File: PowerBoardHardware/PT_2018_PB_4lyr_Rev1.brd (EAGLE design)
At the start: 177.8 x 209.6 mm, 250 parts, among them J1 APP_2POS_CONFIG12V_VERT, J2 APP_2POS_CONFIG12V_VERT, J3 APP_2POS_CONFIG12V_VERT, J4 RJ45KEYSTONE-942, J5 APP_2POS_CONFIGMOCO_VERT, J6 JTAG_ARM_10PIN, Q1 Q_IRFS7437PbF, Q10 Q_IRFS7437PbF, Q11 2N7002, Q12 2N7002, Q13 2N7002PW, Q14 2N7002PW, Q2 Q_IRFS7437PbF, Q3 Q_IRFS7437PbF, Q4 Q_IRFS7437PbF, Q5 MOSFET-NCHANNELFDD8780, Q6 Q_IRFS7437PbF, Q7 Q_IRFS7437PbF, Q8 MOSFET-NCHANNELFDD8780, Q9 Q_IRFS7437PbF, U1 ACS722LLCTR-40AU-T, U10 LT1910, U11 LT1910, U12 ACS722LLCTR-40AU-T, U13 LT1910, U14 ACS722LLCTR-40AU-T, U15 LT1910, U16 LT1910, U17 ACS722LLCTR-40AU-T, U18 ACS722LLCTR-40AU-T, U19 LT1910, U2 ACS722LLCTR-40AU-T, U20 LT1910, U21 SLVU2.8-4, U22 HX1198FNL, U23 MAX3232D, U3 LT1910, U4 ACS722LLCTR-40AU-T, U5 LT1910, U6 ACS722LLCTR-40AU-T, U7 LT1910, U8 ACS722LLCTR-40AU-T, U9 ACS722LLCTR-40AU-T, Y1 CRYATL_32K_SMD, Y2 NX3225GA

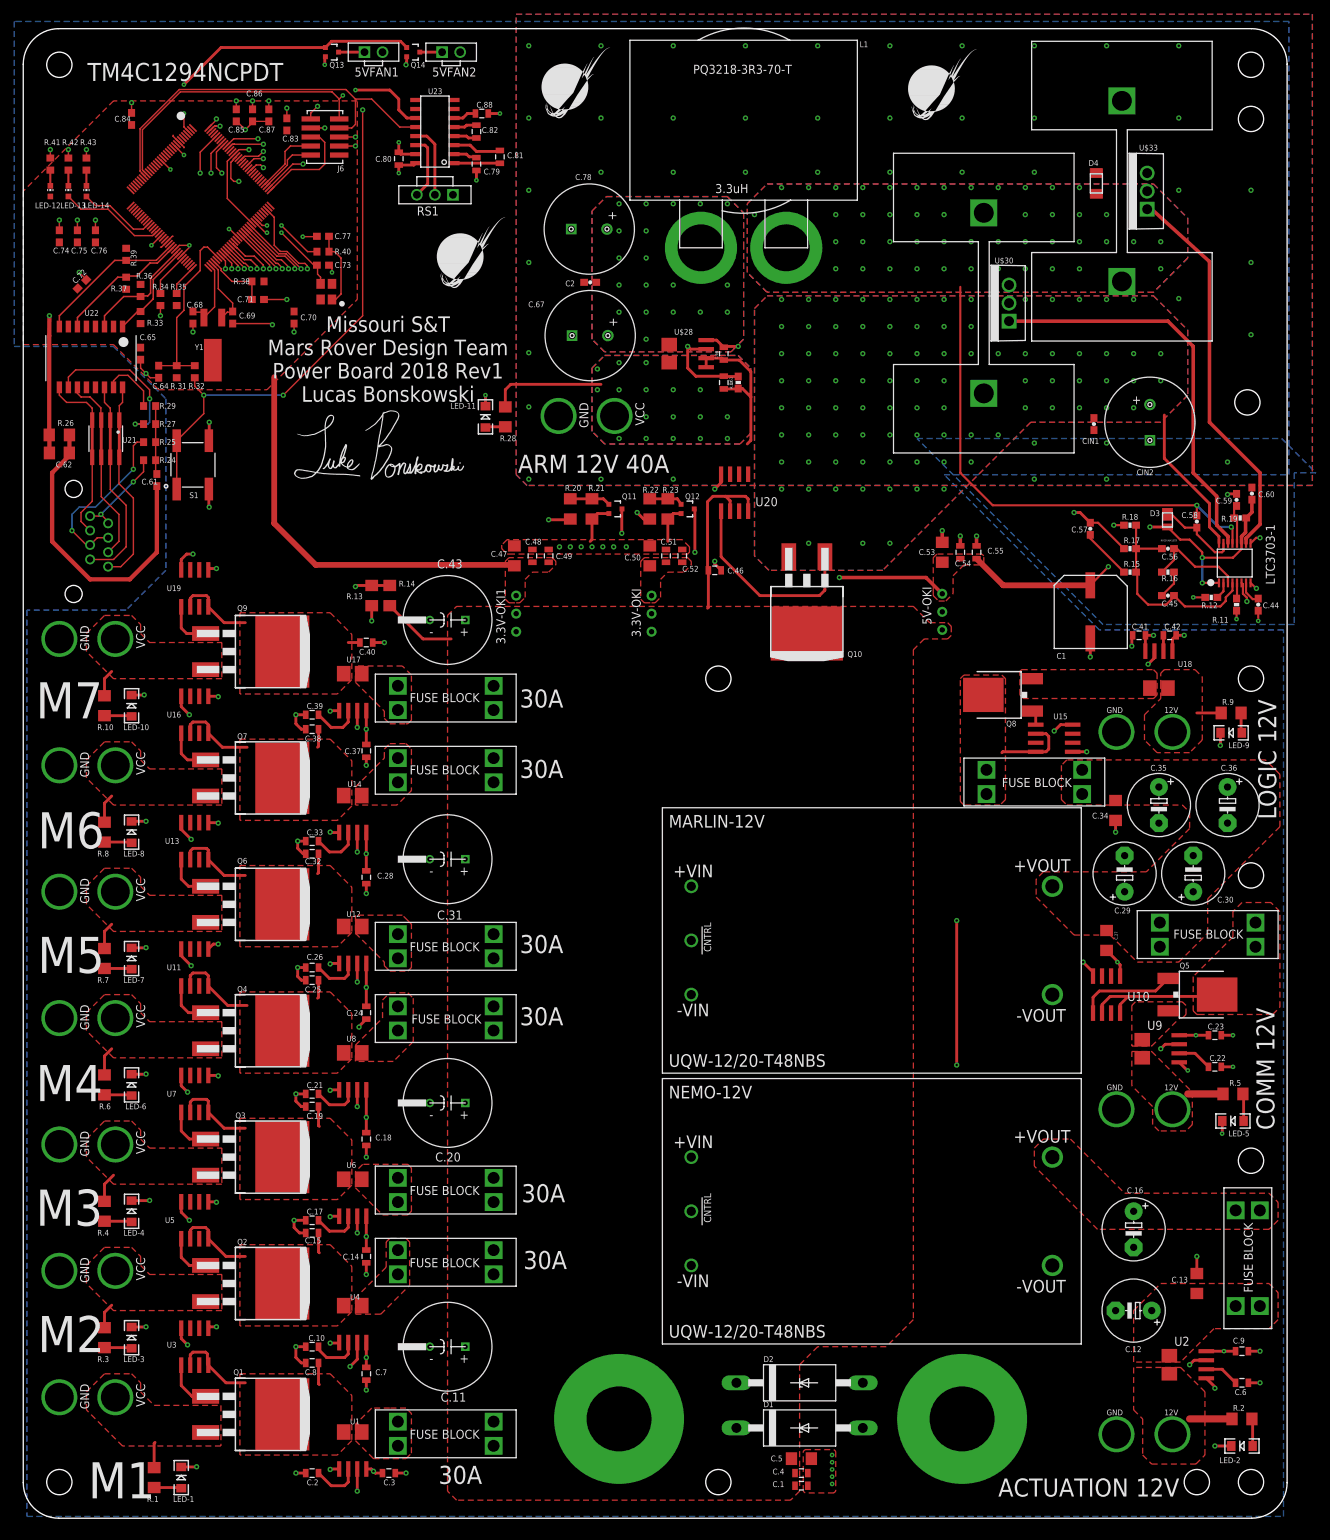
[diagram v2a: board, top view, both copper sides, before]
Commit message: FINAL REV 1 TO BE ORDERED
Made ground plane around buck converter 4 layers. Adjusted via stitch to allow 3.3v plane to have a larger bottleneck.  Flipped logic and comm bus locations.  Added + and - near battery terminals. Renumbered components since we missed a few before.
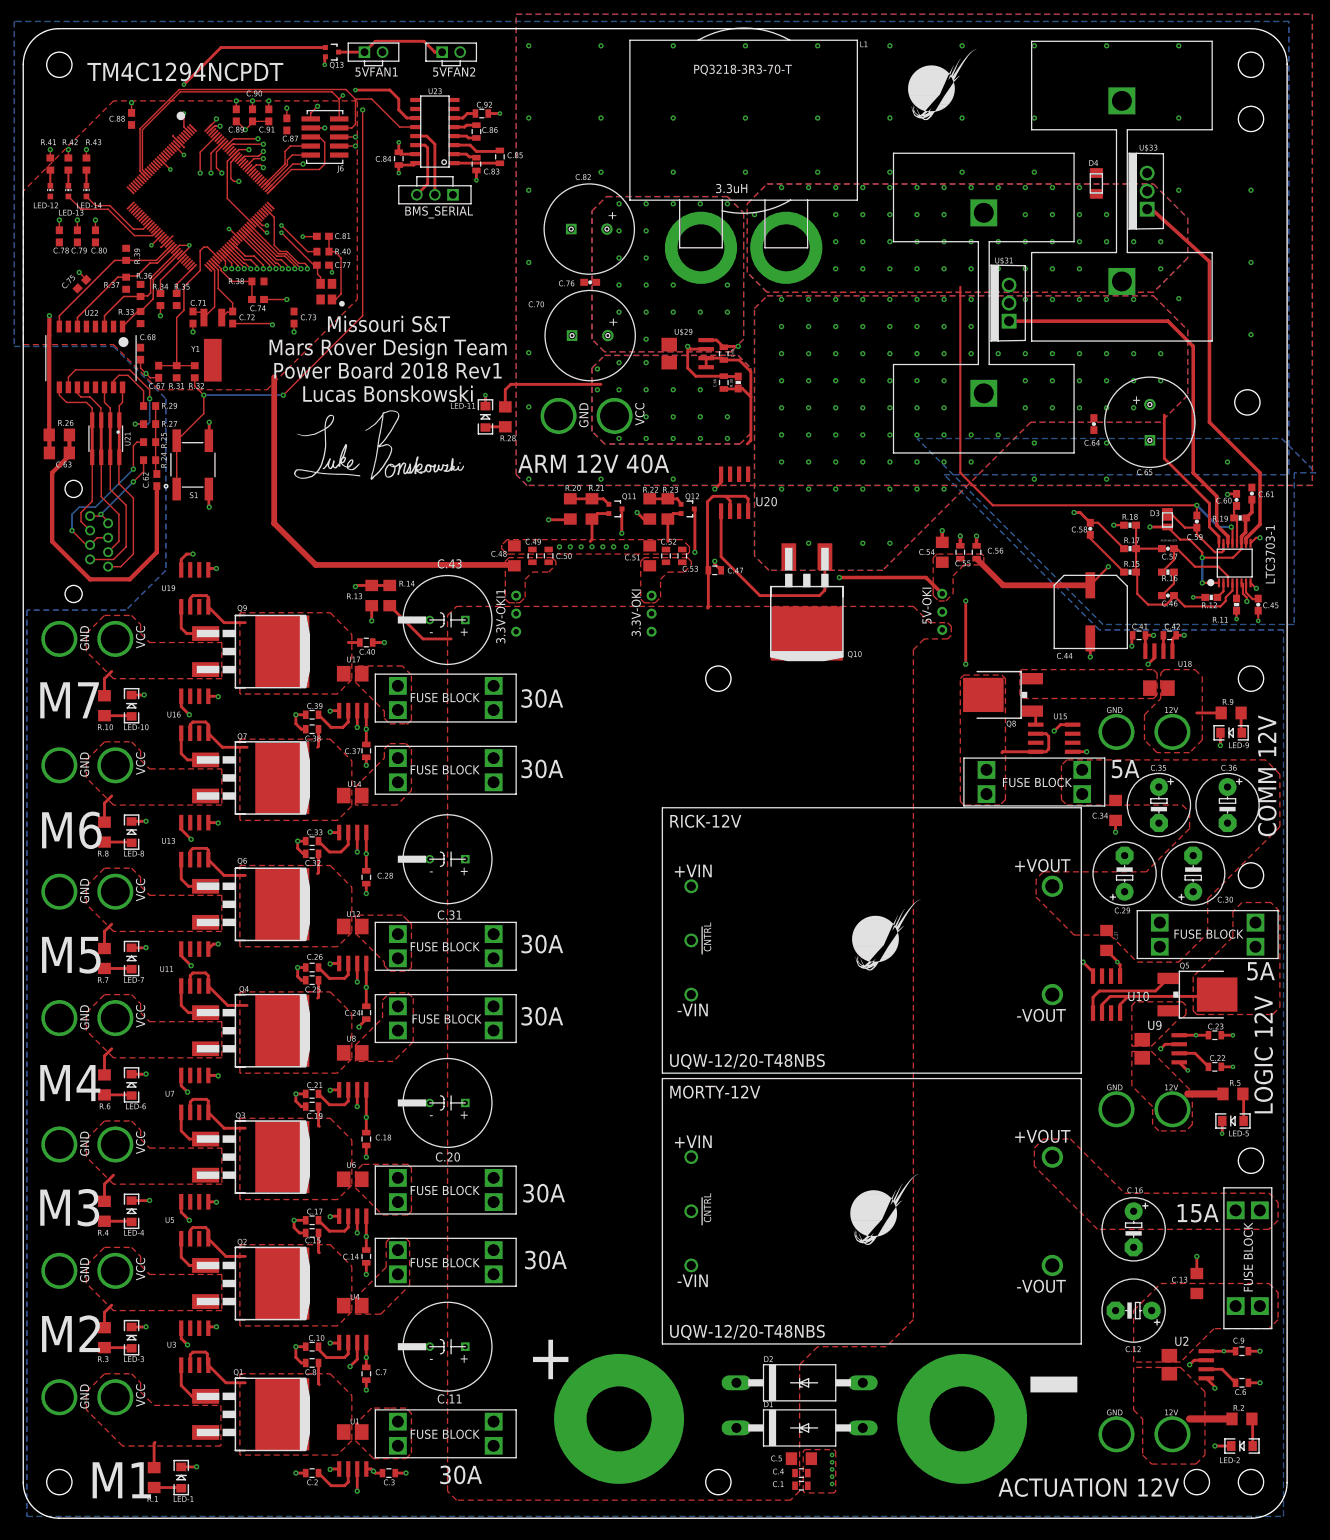
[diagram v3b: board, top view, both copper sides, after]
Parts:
- removed C1: 22u, buckconverter:CAP_POL_22UF
- removed C2: 22p, SparkFun-Passives:0603-CAP
- removed CIN1: 1000p, SparkFun-Passives:0603-CAP
- removed CIN2: 100u, buckconverter:CAP_POL_220UF
- removed Q14: 2N7002PW, SparkFun-DiscreteSemi:SOT323
- added C.89: 2.2uF, resistor:C0603
- added C.90: 0.1uF, resistor:C0603
- added C.91: 1.0uF, resistor:C0603
- added C.92: .1u, SparkFun-Passives:0805
- C.44: value 0.1uF -> 22u; device SparkFun-Passives:0603-CAP -> buckconverter:CAP_POL_22UF
- C.45: value 1000p -> 0.1uF
- C.46: value .1µF -> 1000p; device SparkFun-Capacitors:0805 -> SparkFun-Passives:0603-CAP
- C.47: value 10uF -> .1µF; device SparkFun-Capacitors:1206 -> SparkFun-Capacitors:0805
- C.48, C.51: value 1nF -> 10uF; device SparkFun-Capacitors:0805 -> SparkFun-Capacitors:1206
- C.49, C.52: value .1uF -> 1nF
- C.50, C.53: value 10uF -> .1uF; device SparkFun-Capacitors:1206 -> SparkFun-Capacitors:0805
- C.54: value .1uF -> 10uF; device SparkFun-Capacitors:0805 -> SparkFun-Capacitors:1206
- C.55: value 1nF -> .1uF
- C.56: value 470p -> 1nF; device SparkFun-Passives:0603-CAP -> SparkFun-Capacitors:0805
- C.57: value 2200p -> 470p
- C.58: value 0.1uF -> 2200p
- C.59: value 1uF -> 0.1uF
- C.60: value 10u -> 1uF
- C.61: value 1000pF -> 10u; device resistor:C0603 -> SparkFun-Passives:0603-CAP
- C.62: value 4700pF -> 1000pF; device resistor:C1206 -> resistor:C0603
- C.63: value 10n -> 4700pF; device SparkFun-Capacitors:0805 -> resistor:C1206
- C.64: value 0.1uF -> 1000p; device resistor:C0603 -> SparkFun-Passives:0603-CAP
- C.65: value 0.1uF -> 100u; device resistor:C0603 -> buckconverter:CAP_POL_220UF
- C.66: value .1µF -> 10n
- C.67, C.78: value 220u -> 0.1uF; device buckconverter:CAP_POL_220UF -> resistor:C0603
- C.68, C.73: value 12pF -> 0.1uF
- C.69: value 12pF -> .1µF; device resistor:C0603 -> SparkFun-Capacitors:0805
- C.70: value 0.1uF -> 220u; device resistor:C0603 -> buckconverter:CAP_POL_220UF
- C.71, C.72: value 0.1uF -> 12pF
- C.76: value 0.1uF -> 22p; device resistor:C0603 -> SparkFun-Passives:0603-CAP
- C.79, C.80, C.88: value .1u -> 0.1uF; device SparkFun-Passives:0805 -> resistor:C0603
- C.81: value .1u -> 12pF; device SparkFun-Passives:0805 -> resistor:C0603
- C.82: value .1u -> 220u; device SparkFun-Passives:0805 -> buckconverter:CAP_POL_220UF
- C.83, C.84, C.86: value 0.1uF -> .1u; device resistor:C0603 -> SparkFun-Passives:0805
- C.85: value 2.2uF -> .1u; device resistor:C0603 -> SparkFun-Passives:0805
- C.87: value 1.0uF -> 0.1uF
- U$11, U$17: value MOUNTING_HOLE#6 -> ATC_FUSE_BLOCK; device MRDT-Hardware:#6_SCREW -> MRDT-Hardware:BLOCK_3557-2
- U$12, U$18: value APP_2POS_CONFIGMOCO_VERT -> MOUNTING_HOLE#6; device MRDT-Connectors:APP45_MOCO_VERT_CONFIG -> MRDT-Hardware:#6_SCREW
- U$13, U$15, U$19, U$9: value ATC_FUSE_BLOCK -> APP_2POS_CONFIGMOCO_VERT; device MRDT-Hardware:BLOCK_3557-2 -> MRDT-Connectors:APP45_MOCO_VERT_CONFIG
- U$14, U$21, U$25: value APP_2POS_CONFIGMOCO_VERT -> ATC_FUSE_BLOCK; device MRDT-Connectors:APP45_MOCO_VERT_CONFIG -> MRDT-Hardware:BLOCK_3557-2
- U$22: value MOUNTING_HOLE#6 -> APP_2POS_CONFIGMOCO_VERT; device MRDT-Hardware:#6_SCREW -> MRDT-Connectors:APP45_MOCO_VERT_CONFIG
- U$24: value ATC_FUSE_BLOCK -> MOUNTING_HOLE#6; device MRDT-Hardware:BLOCK_3557-2 -> MRDT-Hardware:#6_SCREW
- U$26: value LUCAS_BONSKOWSKI_SIGNATURE -> APP_2POS_CONFIGMOCO_VERT; device MRDT-Signatures:LUCAS_BONSKOWSKI_SIGNATURE -> MRDT-Connectors:APP45_MOCO_VERT_CONFIG
- U$27: value MOUNTING_HOLE#6 -> LUCAS_BONSKOWSKI_SIGNATURE; device MRDT-Hardware:#6_SCREW -> MRDT-Signatures:LUCAS_BONSKOWSKI_SIGNATURE
- U$28: value MLX91210 -> MOUNTING_HOLE#6; device buckconverter:SOIC8_ACS711 -> MRDT-Hardware:#6_SCREW
- U$29: value 530002B02500G -> MLX91210; device buckconverter:RADIAL_FIN_HEATSINK -> buckconverter:SOIC8_ACS711
- U$30: value IPP052N06L3GXKSA1 -> 530002B02500G; device buckconverter:TO-220 -> buckconverter:RADIAL_FIN_HEATSINK
- U$31: value MRDT_LOGO -> IPP052N06L3GXKSA1; device MRDT-2015-General:MRDT_LOGO -> buckconverter:TO-220
- U$8: value APP_2POS_CONFIGMOCO_VERT -> MRDT_LOGO; device MRDT-Connectors:APP45_MOCO_VERT_CONFIG -> MRDT-2015-General:MRDT_LOGO
- moved U$15 174.7 mm to (1.91, 74.3), turned to 270 degrees
- moved U$12 170.9 mm to (172.7, 50.3), turned to 0 degrees
- moved U$18 170.8 mm to (172.7, 90.4), turned to 0 degrees
- moved C.61 154.1 mm to (172.8, 144.1), turned to 90 degrees
- moved C.65 142.3 mm to (158.5, 154.2), turned to 0 degrees
- moved U$27 134.9 mm to (37.8, 145.5)
- moved C.64 131.8 mm to (150.6, 153.9)
- moved U$19 131.3 mm to (1.91, 92.1), turned to 270 degrees
- moved LOGO1 127.6 mm to (116.6, 76.2)
- moved U$16 127.1 mm to (176.5, 78.7), turned to 180 degrees
- moved U$17 123.4 mm to (49.5, 83.8)
- moved U$11 123.2 mm to (49.5, 49.5)
- moved U$24 123.2 mm to (172.7, 118.1)
- moved U$8 114.4 mm to (116.3, 37.6), turned to 0 degrees
- moved U$22 96.2 mm to (1.91, 109.9), turned to 270 degrees
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- renumbered MARLIN-12V to RICK-12V, NEMO-12V to MORTY-12V, RS1 to BMS_SERIAL
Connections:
- removed net N$13: 5VFAN2.1, Q14.3
- net +3V3: now also C.50.1, C.68.1, C.73.1, C.78.1, C.79.1, C.80.1, C.87.1, C.88.1; no longer C.47.1, C.65.1, C.70.1, C.72.1, C.74.1, C.76.1, C.83.1, C.84.1
- net 3.3V: now also C.53.1, C.84.1; no longer C.50.1, C.80.1
- net 5V: now also C.44.+, C.56.1, C.61.1, C.69.2, U$29.8; no longer C.53.1, C.60.1, C.66.2, C1.+, U$28.8
- net ARM-BUS: now also U$29.4; no longer U$28.4
- net FAN_CTL_1: no longer Q14.1
- net GND: now also C.44.-, C.45.2, C.47.1, C.56.2, C.61.2, C.65.GND, C.66.2, C.67.2, C.69.1, C.70.GND, C.78.2, C.81.2, C.82.GND, C.89.2, C.90.2, C.91.2, C.92.2, U$13.GND, U$15.GND, U$19.GND, U$22.GND, U$26.GND, U$29.5, U$29.6, U$9.GND; no longer C.44.2, C.46.1, C.47.2, C.59.2, C.62.2, C.65.2, C.66.1, C.67.GND, C.69.2, C.70.2, C.78.GND, C.85.2, C.86.2, C1.-, C2.2, CIN1.2, CIN2.GND, Q14.2, U$12.GND, U$14.GND, U$18.GND, U$21.GND, U$25.GND, U$28.5, U$28.6, U$8.GND
- net IMEAS-ARM: now also C.66.1, U$29.7; no longer C.63.1, U$28.7
- net N$11: now also C.83.1; no longer C.79.1
- net N$14: now also C.45.1; no longer C.44.1
- net N$20: now also U$20.OUT_1, U$20.OUT_2; no longer U$19.OUT_1, U$19.OUT_2
- net N$21: now also U$16.OUT_1, U$16.OUT_2; no longer U$15.OUT_1, U$15.OUT_2
- net N$23: now also C.57.1; no longer C.56.1
- net N$24: now also C.46.1; no longer C.45.1
- net N$26: now also C.58.1; no longer C.57.1
- net N$27: now also C.46.2, C.57.2; no longer C.45.2, C.56.2
- net N$29: now also C.60.1; no longer C.59.1
- net N$31: now also C.59.2, U$31.3; no longer C.58.2, U$30.3
- net N$32: now also C.59.1; no longer C.58.1
- net N$33: now also U$31.1; no longer U$30.1
- net N$40: now also C.85.1; no longer C.81.1
- net N$42: now also C.85.2; no longer C.81.2
- net N$43: now also C.86.1; no longer C.82.1
- net N$44: now also C.86.2; no longer C.82.2
- net N$45: now also C.92.1; no longer C.88.1
- net N$5: now also 5VFAN2.1
- net N$9: now also U$16.IN_1, U$16.IN_2, U$20.IN_1, U$20.IN_2; no longer U$15.IN_1, U$15.IN_2, U$19.IN_1, U$19.IN_2
- net N_$10: now also C.74.1; no longer C.71.1
- net N_$14: now also C.62.1; no longer C.61.1
- net N_$15: now also C.62.2, C.63.1; no longer C.61.2, C.62.1
- net N_$16: now also C.89.1, C.90.1, C.91.1; no longer C.85.1, C.86.1, C.87.1
- net N_$18: now also C.77.1; no longer C.73.1
- net N_$20: now also C.67.1; no longer C.64.1
- net N_$21: now also C.81.1; no longer C.77.1
- net N_$22: now also C.72.1; no longer C.69.1
- net N_$23: now also C.71.1; no longer C.68.1
- net SOURCE-ARM: now also C.64.1, C.65.+, U$31.2; no longer CIN1.1, CIN2.+, U$30.2
- net SOURCE-M2: now also U$9.VCC; no longer U$8.VCC
- net SOURCE-M3: now also U$13.VCC; no longer U$12.VCC
- net SOURCE-M4: now also U$15.VCC; no longer U$14.VCC
- net SOURCE-M5: now also U$19.VCC; no longer U$18.VCC
- net SOURCE-M6: now also U$22.VCC; no longer U$21.VCC
- net SOURCE-M7: now also U$26.VCC; no longer U$25.VCC
- net VOUT12+: now also C.58.2, C.70.+, C.76.1, C.82.+, U$29.1; no longer C.57.2, C.67.+, C.78.+, C2.1, U$28.1
- net V_BATT: now also C.47.2, U$11.IN_1, U$11.IN_2, U$14.IN_1, U$14.IN_2, U$17.IN_1, U$17.IN_2, U$21.IN_1, U$21.IN_2, U$25.IN_1, U$25.IN_2; no longer C.46.2, U$13.IN_1, U$13.IN_2, U$16.IN_1, U$16.IN_2, U$20.IN_1, U$20.IN_2, U$24.IN_1, U$24.IN_2, U$9.IN_1, U$9.IN_2
- net V_BATT_M2: now also U$10.OUT_1, U$10.OUT_2; no longer U$9.OUT_1, U$9.OUT_2
- net V_BATT_M3: now also U$11.OUT_1, U$11.OUT_2; no longer U$10.OUT_1, U$10.OUT_2
- net V_BATT_M4: now also U$14.OUT_1, U$14.OUT_2; no longer U$13.OUT_1, U$13.OUT_2
- net V_BATT_M5: now also U$17.OUT_1, U$17.OUT_2; no longer U$16.OUT_1, U$16.OUT_2
- net V_BATT_M6: now also U$21.OUT_1, U$21.OUT_2; no longer U$20.OUT_1, U$20.OUT_2
- net V_BATT_M7: now also U$25.OUT_1, U$25.OUT_2; no longer U$24.OUT_1, U$24.OUT_2
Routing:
- net N$5: track 3.65 -> 15.8 mm
- net FAN_CTL_1: track 41.2 -> 29.0 mm
- net N$13: track 3.14 -> 0.00 mm
- net IMEAS-COM: track 184.1 -> 186.2 mm
- net GND: track 253.6 -> 252.4 mm, vias 157 -> 156
- net IMEAS-ACT: track 279.8 -> 280.8 mm
- added copper zone on layer 15, net GND
- added copper zone on layer 2, net GND
- added copper zone on layer 2, net V_BATT
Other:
- board text added: "+"
- board text added: "-"
- board text added: "15A"
- board text added: "5A"
